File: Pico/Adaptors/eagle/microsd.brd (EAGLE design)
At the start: 23.8 x 17.8 mm, 3 parts

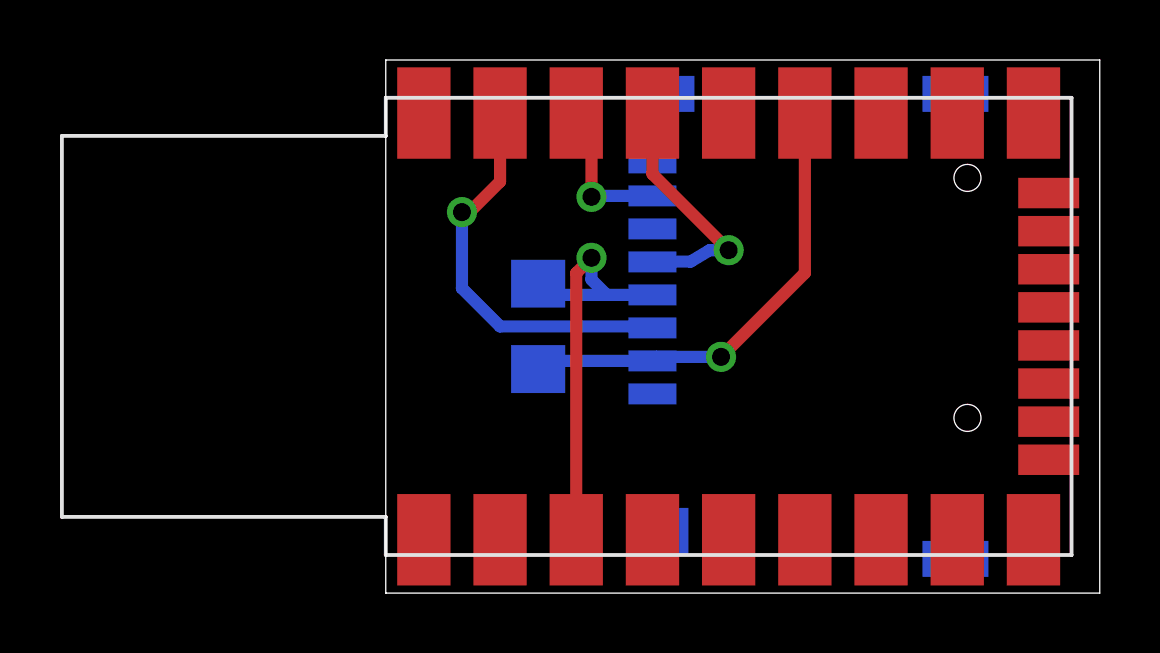
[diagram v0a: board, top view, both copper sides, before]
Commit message: nrf24 adaptor, and DRC
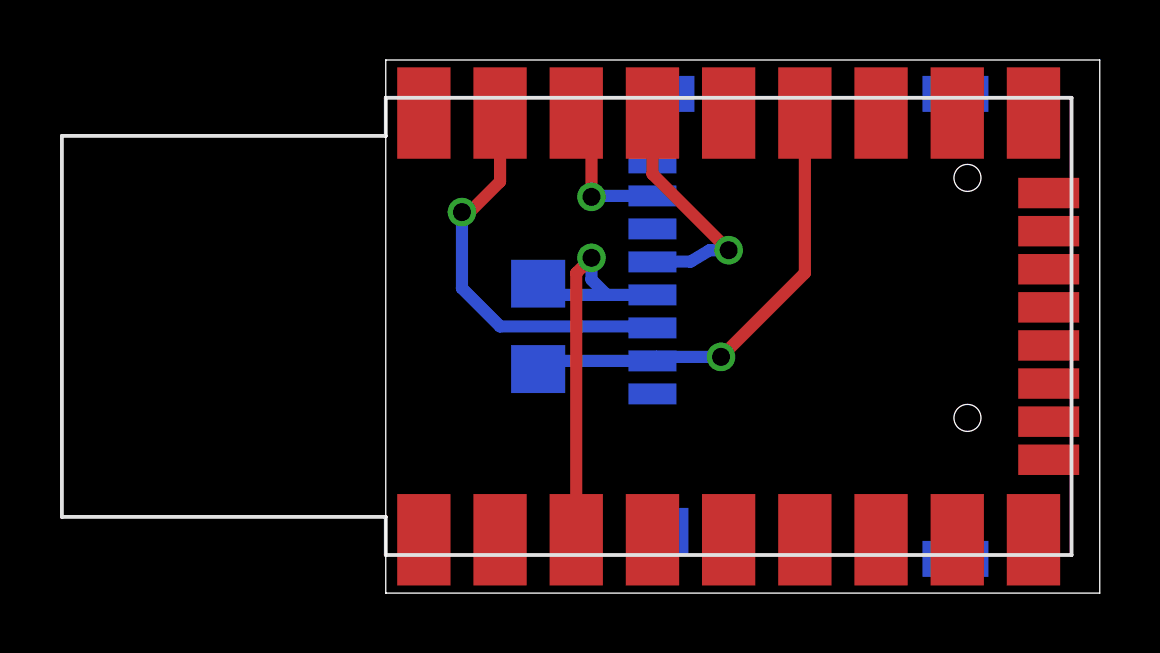
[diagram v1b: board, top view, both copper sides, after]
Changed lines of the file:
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@@
 </class>
 </classes>
-<designrules name="default">
+<designrules name="oshpark-2layer">
 <description language="de">&lt;b&gt;EAGLE Design Rules&lt;/b&gt;
 &lt;p&gt;
@@
 Einstellungen hier und speichern die Design Rules unter
 einem neuen Namen ab.</description>
-<description language="en">&lt;b&gt;EAGLE Design Rules&lt;/b&gt;
+<description language="en">&lt;b&gt;Laen's PCB Order Design Rules&lt;/b&gt;
 &lt;p&gt;
-The default Design Rules have been set to cover
-a wide range of applications. Your particular design
-may have different requirements, so please make the
-necessary adjustments and save your customized
-design rules under a new name.</description>
+Please make sure your boards conform to these design rules.</description>
 <param name="layerSetup" value="(1*16)"/>
-<param name="mtCopper" value="0.035mm 0.035mm 0.035mm 0.035mm 0.035mm 0.035mm 0.035mm 0.035mm 0.035mm 0.035mm 0.035mm 0.035mm 0.035mm 0.035mm 0.035mm 0.035mm"/>
-<param name="mtIsolate" value="1.5mm 0.15mm 0.2mm 0.15mm 0.2mm 0.15mm 0.2mm 0.15mm 0.2mm 0.15mm 0.2mm 0.15mm 0.2mm 0.15mm 0.2mm"/>
-<param name="mdWireWire" value="8mil"/>
-<param name="mdWirePad" value="8mil"/>
-<param name="mdWireVia" value="8mil"/>
-<param name="mdPadPad" value="8mil"/>
-<param name="mdPadVia" value="8mil"/>
-<param name="mdViaVia" value="8mil"/>
-<param name="mdSmdPad" value="8mil"/>
-<param name="mdSmdVia" value="8mil"/>
-<param name="mdSmdSmd" value="8mil"/>
+<param name="mtCopper" value="0.0356mm 0.0356mm 0.0356mm 0.0356mm 0.0356mm 0.0356mm 0.0356mm 0.0356mm 0.0356mm 0.0356mm 0.0356mm 0.0356mm 0.0356mm 0.0356mm 0.0356mm 0.0356mm"/>
+<param name="mtIsolate" value="1.5011mm 0.1499mm 0.2007mm 0.1499mm 0.2007mm 0.1499mm 0.2007mm 0.1499mm 0.2007mm 0.1499mm 0.2007mm 0.1499mm 0.2007mm 0.1499mm 0.2007mm"/>
+<param name="mdWireWire" value="6mil"/>
+<param name="mdWirePad" value="6mil"/>
+<param name="mdWireVia" value="6mil"/>
+<param name="mdPadPad" value="6mil"/>
+<param name="mdPadVia" value="6mil"/>
+<param name="mdViaVia" value="6mil"/>
+<param name="mdSmdPad" value="6mil"/>
+<param name="mdSmdVia" value="6mil"/>
+<param name="mdSmdSmd" value="6mil"/>
 <param name="mdViaViaSameLayer" value="8mil"/>
 <param name="mnLayersViaInSmd" value="2"/>
-<param name="mdCopperDimension" value="40mil"/>
-<param name="mdDrill" value="8mil"/>
+<param name="mdCopperDimension" value="15mil"/>
+<param name="mdDrill" value="6mil"/>
 <param name="mdSmdStop" value="0mil"/>
-<param name="msWidth" value="10mil"/>
-<param name="msDrill" value="24mil"/>
-<param name="msMicroVia" value="9.99mm"/>
+<param name="msWidth" value="6mil"/>
+<param name="msDrill" value="13mil"/>
+<param name="msMicroVia" value="13mil"/>
 <param name="msBlindViaRatio" value="0.5"/>
 <param name="rvPadTop" value="0.25"/>
@@
 <param name="rvMicroViaOuter" value="0.25"/>
 <param name="rvMicroViaInner" value="0.25"/>
-<param name="rlMinPadTop" value="10mil"/>
+<param name="rlMinPadTop" value="7mil"/>
 <param name="rlMaxPadTop" value="20mil"/>
-<param name="rlMinPadInner" value="10mil"/>
+<param name="rlMinPadInner" value="7mil"/>
 <param name="rlMaxPadInner" value="20mil"/>
-<param name="rlMinPadBottom" value="10mil"/>
+<param name="rlMinPadBottom" value="7mil"/>
 <param name="rlMaxPadBottom" value="20mil"/>
-<param name="rlMinViaOuter" value="8mil"/>
+<param name="rlMinViaOuter" value="7mil"/>
 <param name="rlMaxViaOuter" value="20mil"/>
-<param name="rlMinViaInner" value="8mil"/>
+<param name="rlMinViaInner" value="7mil"/>
 <param name="rlMaxViaInner" value="20mil"/>
 <param name="rlMinMicroViaOuter" value="4mil"/>
